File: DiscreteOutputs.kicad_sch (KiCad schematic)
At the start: 35 parts, among them Q13 BC817, Q14 BC817, Q15 BC817, Q16 BC817, Q17 BC817, U50 ACPL-M50L, U51 PVG612, U52 PVG612, U53 PVG612, U54 PVG612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

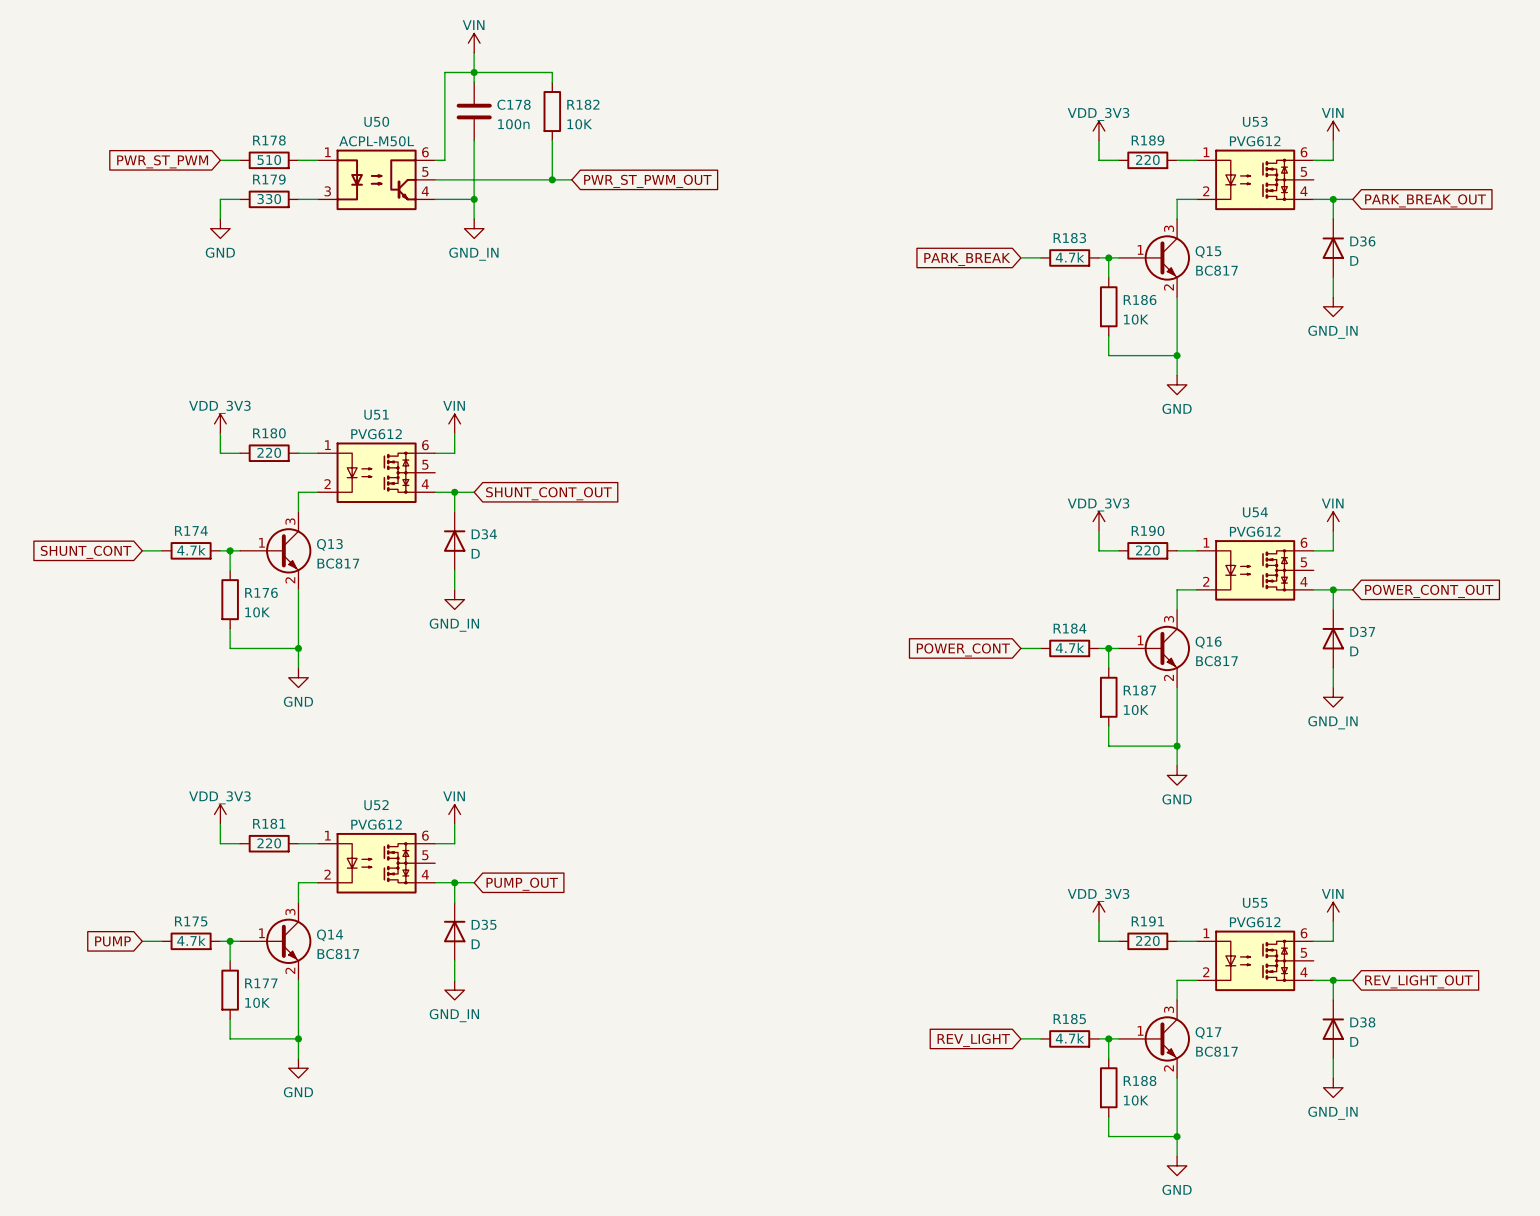
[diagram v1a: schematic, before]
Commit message: Изменения: добавл BOM, оформляю заказ
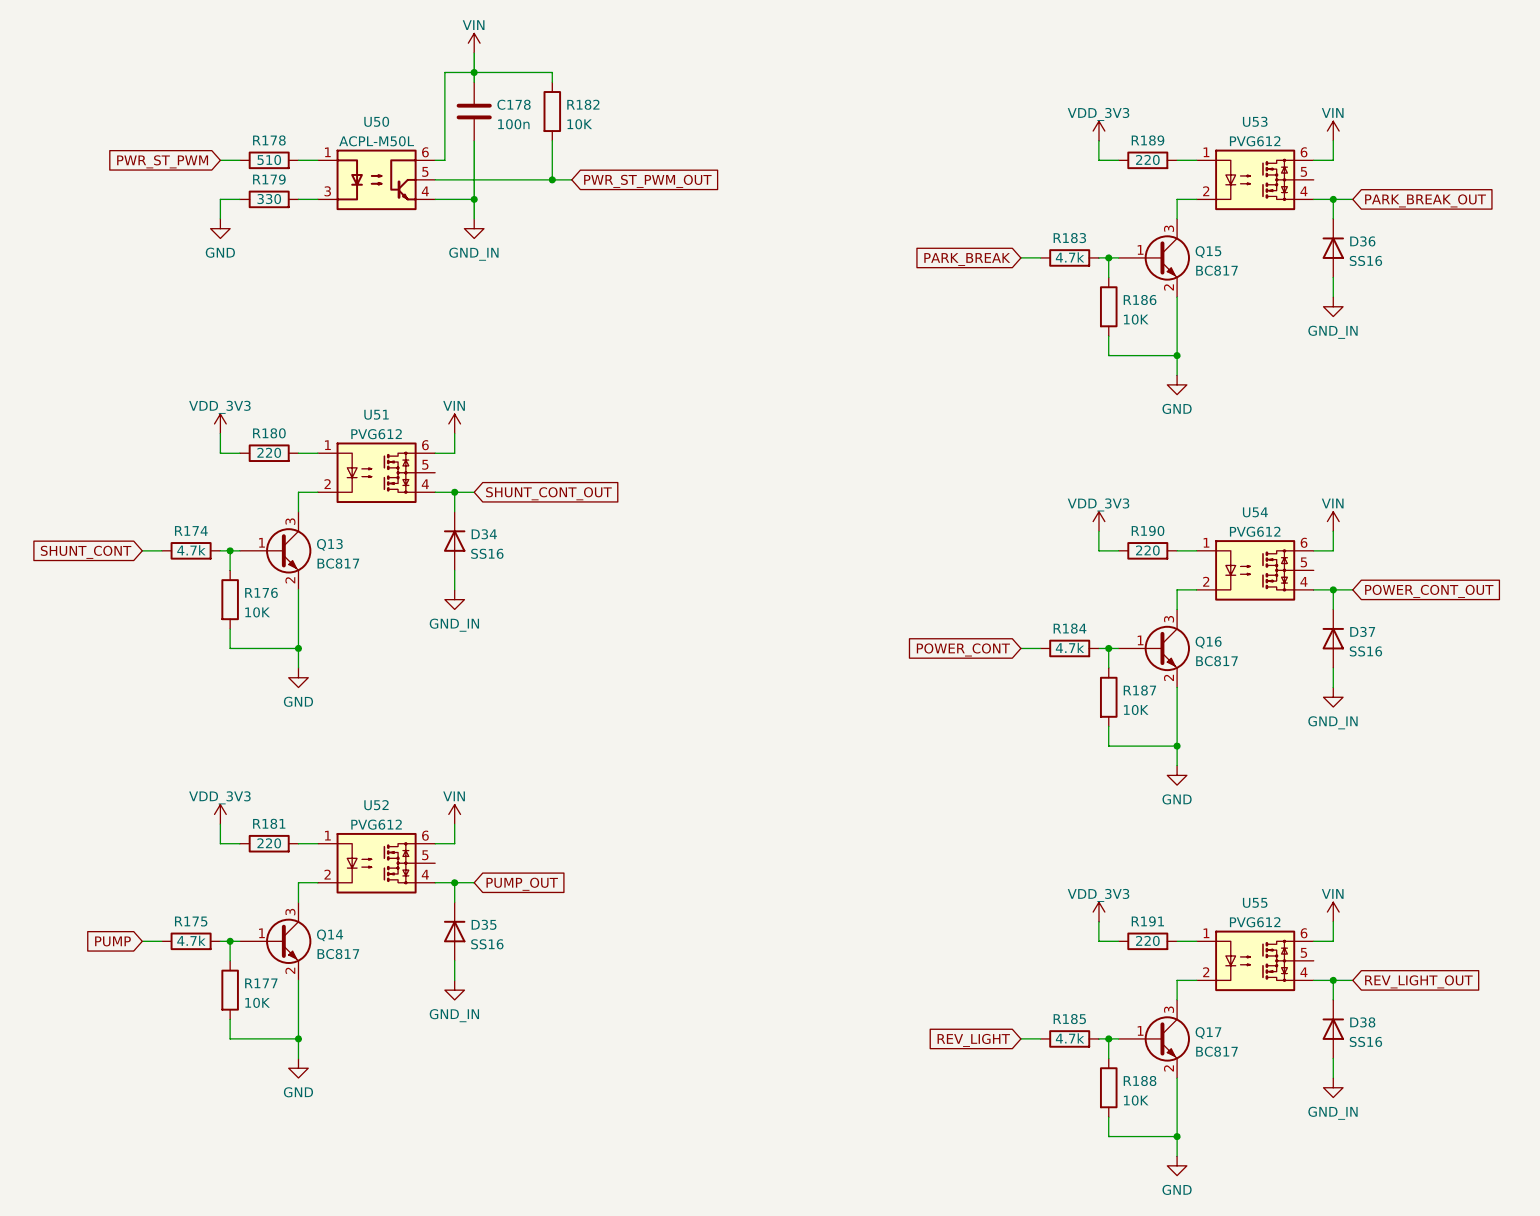
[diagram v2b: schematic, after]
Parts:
- D34, D35, D36, D37, D38: value D -> SS16
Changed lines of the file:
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@@
 			)
 		)
-		(property "Value" "D"
+		(property "Value" "SS16"
 			(at 196.342 105.8422 90)
 			(effects
@@
 			)
 		)
-		(property "Value" "D"
+		(property "Value" "SS16"
 			(at 82.042 93.1422 90)
 			(effects
@@
 			)
 		)
-		(property "Value" "D"
+		(property "Value" "SS16"
 			(at 196.342 55.0422 90)
 			(effects
@@
 			)
 		)
-		(property "Value" "D"
+		(property "Value" "SS16"
 			(at 196.342 156.6422 90)
 			(effects
@@
 			)
 		)
-		(property "Value" "D"
+		(property "Value" "SS16"
 			(at 82.042 143.9422 90)
 			(effects
